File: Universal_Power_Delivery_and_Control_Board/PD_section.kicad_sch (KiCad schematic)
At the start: 76 parts, among them Q1 PMZ600UNEYL, Q2 PMZ600UNEYL, U1 TPS259470LRPWR, U2 CH224Q_C46061833, U21 TPS22919DCK, U26 TPS2116DRL, U3 USBLC6-2SC6, U4 ESD2CAN24-ES, U5 S2B-ZR (LF)(SN), U6 USBLC6-2SC6, U7 TPS54202DDC

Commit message: Minor layout fixes to the UPDBC.
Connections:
- net H_current: now also R38.2; no longer R37.2
- net MAX_current: now also R37.2; no longer R38.2
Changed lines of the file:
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@@
 	(hierarchical_label "H_current"
 		(shape input)
-		(at 143.51 91.44 0)
+		(at 143.51 102.87 0)
 		(effects
 			(font
@@
 	(hierarchical_label "MAX_current"
 		(shape input)
-		(at 143.51 102.87 0)
+		(at 143.51 91.44 0)
 		(effects
 			(font

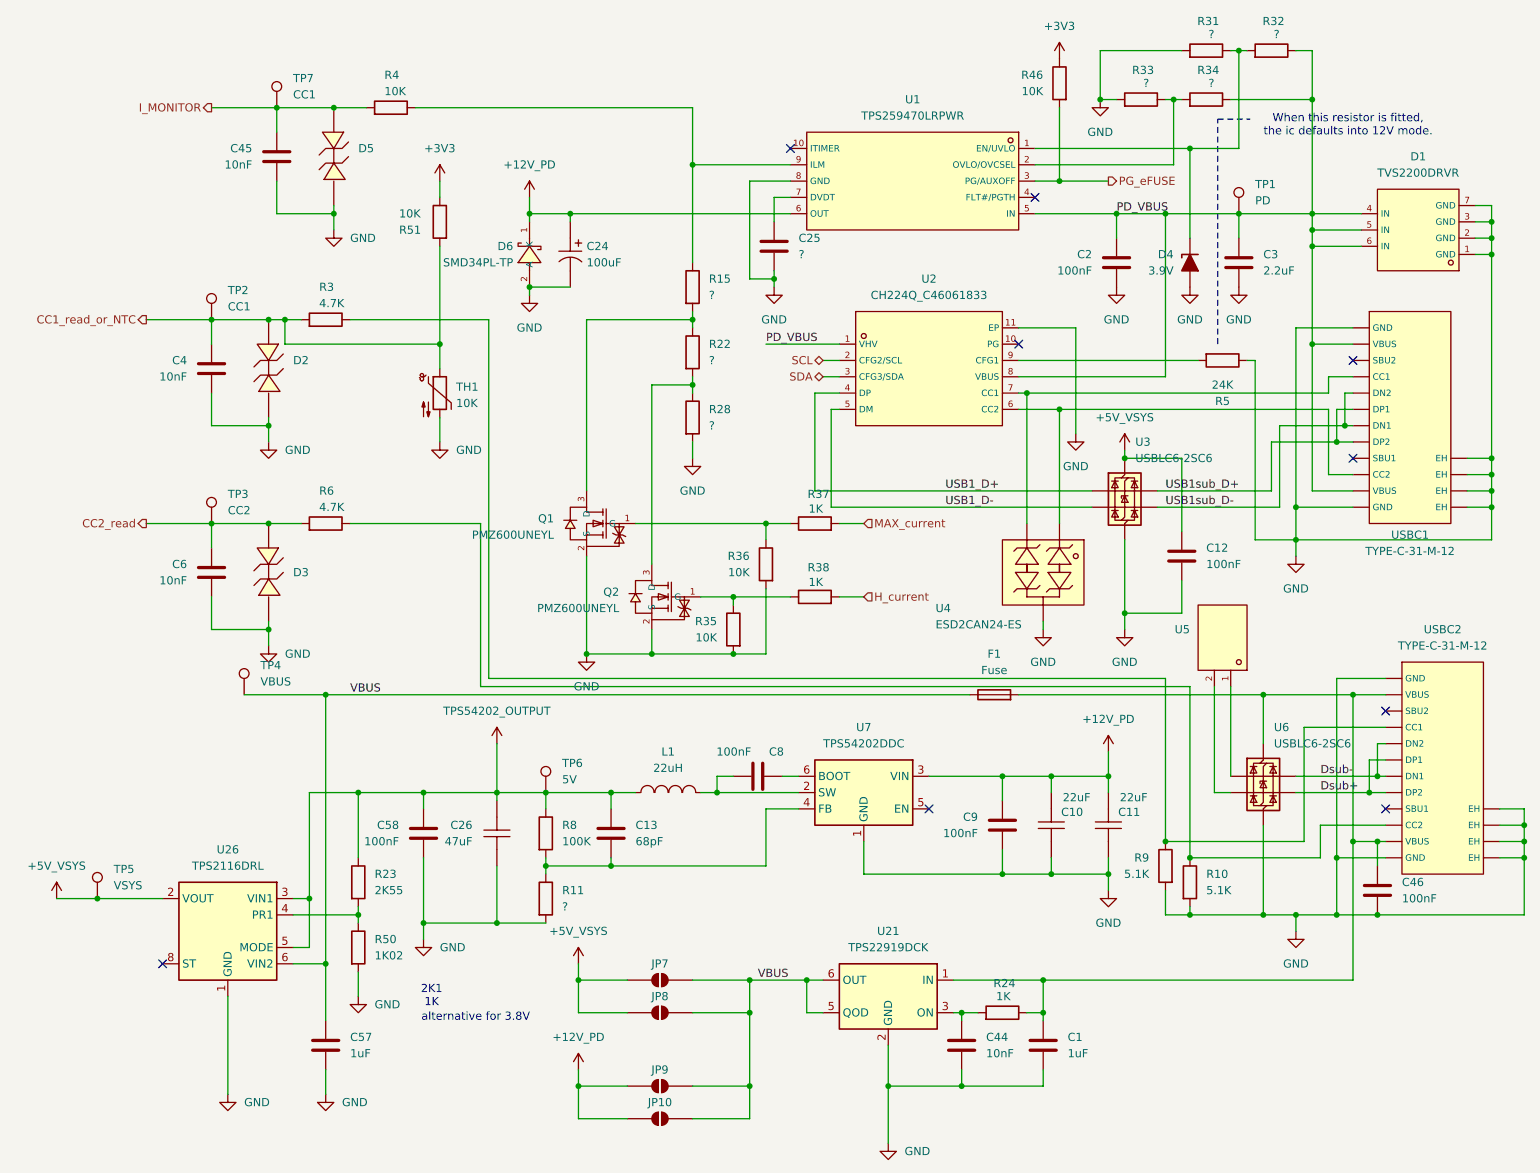
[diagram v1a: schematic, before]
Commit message: Small mostly cosmetic changes and reannotation of the schematic, followed by the export of the gerber files for production.
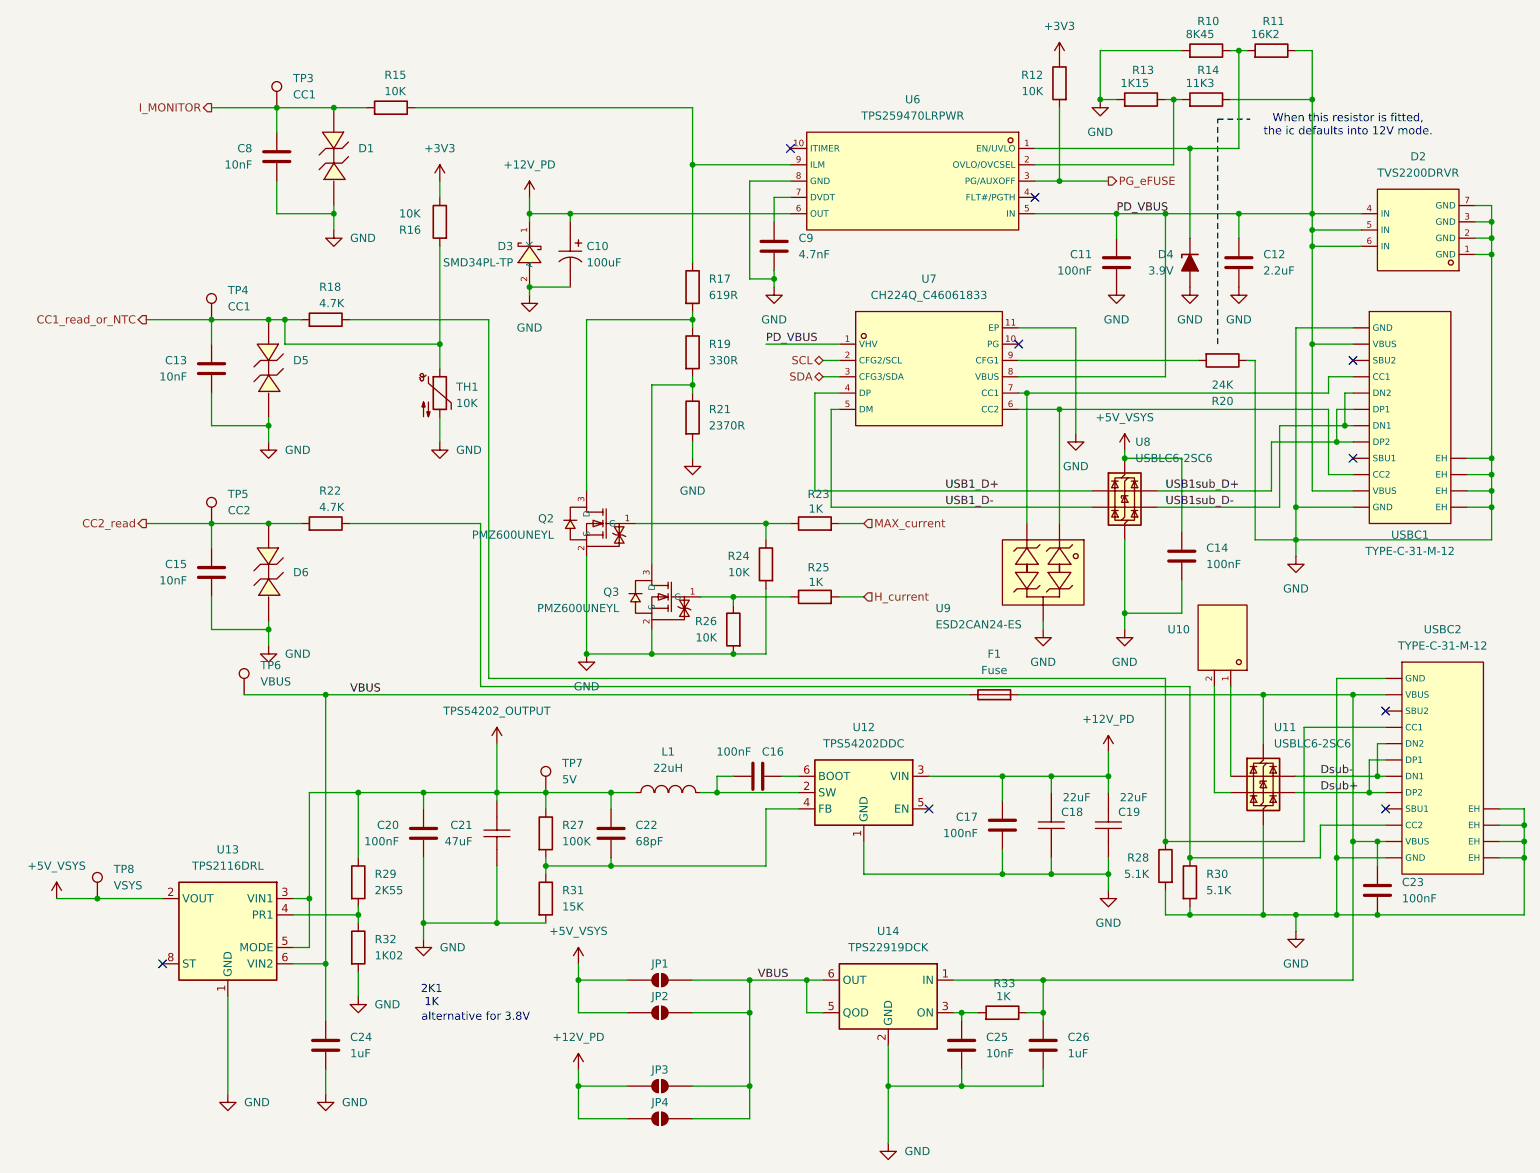
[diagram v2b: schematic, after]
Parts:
- removed TP1: PD, TestPoint:TestPoint_Pad_D1.0mm, symbol Connector:TestPoint
- C9: renamed from C25; value ? -> 4.7nF
- R10: renamed from R31; value ? -> 8K45
- R11: renamed from R32; value ? -> 16K2
- R13: renamed from R33; value ? -> 1K15
- R14: renamed from R34; value ? -> 11K3
- R17: renamed from R15; value ? -> 619R
- R19: renamed from R22; value ? -> 330R
- R21: renamed from R28; value ? -> 2370R
- R31: renamed from R11; value ? -> 15K
- renumbered C24 to C10, C2 to C11, C3 to C12, C4 to C13, C12 to C14, C6 to C15, C8 to C16, C9 to C17, C10 to C18, C11 to C19, C58 to C20, C26 to C21, C13 to C22, C46 to C23, C57 to C24, C44 to C25, C1 to C26, C45 to C8, D5 to D1, D1 to D2, D6 to D3, D2 to D5, D3 to D6, JP7 to JP1, JP8 to JP2, JP9 to JP3, JP10 to JP4, Q1 to Q2, Q2 to Q3, R46 to R12, R4 to R15, R51 to R16, R3 to R18, R5 to R20, R6 to R22, R37 to R23, R36 to R24, R38 to R25, R35 to R26, R8 to R27, R9 to R28, R23 to R29, R10 to R30, R50 to R32, R24 to R33, TP7 to TP3, TP2 to TP4, TP3 to TP5, TP4 to TP6, TP6 to TP7, TP5 to TP8, U5 to U10, U6 to U11, U7 to U12, U26 to U13, U21 to U14, U1 to U6, U2 to U7, U3 to U8, U4 to U9
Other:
- company: (none) -> Jan Ścibielski
- title: (none) -> PD section
